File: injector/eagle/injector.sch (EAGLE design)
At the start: 30 parts, among them U1 ATMEGA328, U2 ATA6631, U3 ATA6631, X1 16MHz

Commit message: Renamed proxy to injector.
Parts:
- C1, C3, C4, C6, C7, C8, C9: device proxy:C-USC0805 -> injector:C-USC0805
- C2: device proxy:CPOL-USUD-6,3X5,8 -> injector:CPOL-USUD-6,3X5,8
- C5: device proxy:CPOL-USA/3216-18R -> injector:CPOL-USA/3216-18R
- D2, D3, D6, D9: device proxy:SMF5.0AT1 -> injector:SMF5.0AT1
- F1: device proxy:FUSE -> injector:FUSE
- J3: device proxy:PINHD-1X6 -> injector:PINHD-1X6
- JP1, JP3: device proxy:PINHD-1X3 -> injector:PINHD-1X3
- JP2: device proxy:PINHD-2X3 -> injector:PINHD-2X3
- LED1, LED2: device proxy:LED -> injector:LED
- R1, R2, R3, R4, R5, R9: device proxy:R-US_R0805 -> injector:R-US_R0805
- U1: device proxy:ATMEGA328 -> injector:ATMEGA328
- U2, U3: device proxy:ATA6631 -> injector:ATA6631
- X1: device proxy:RESONATORSMD -> injector:RESONATORSMD

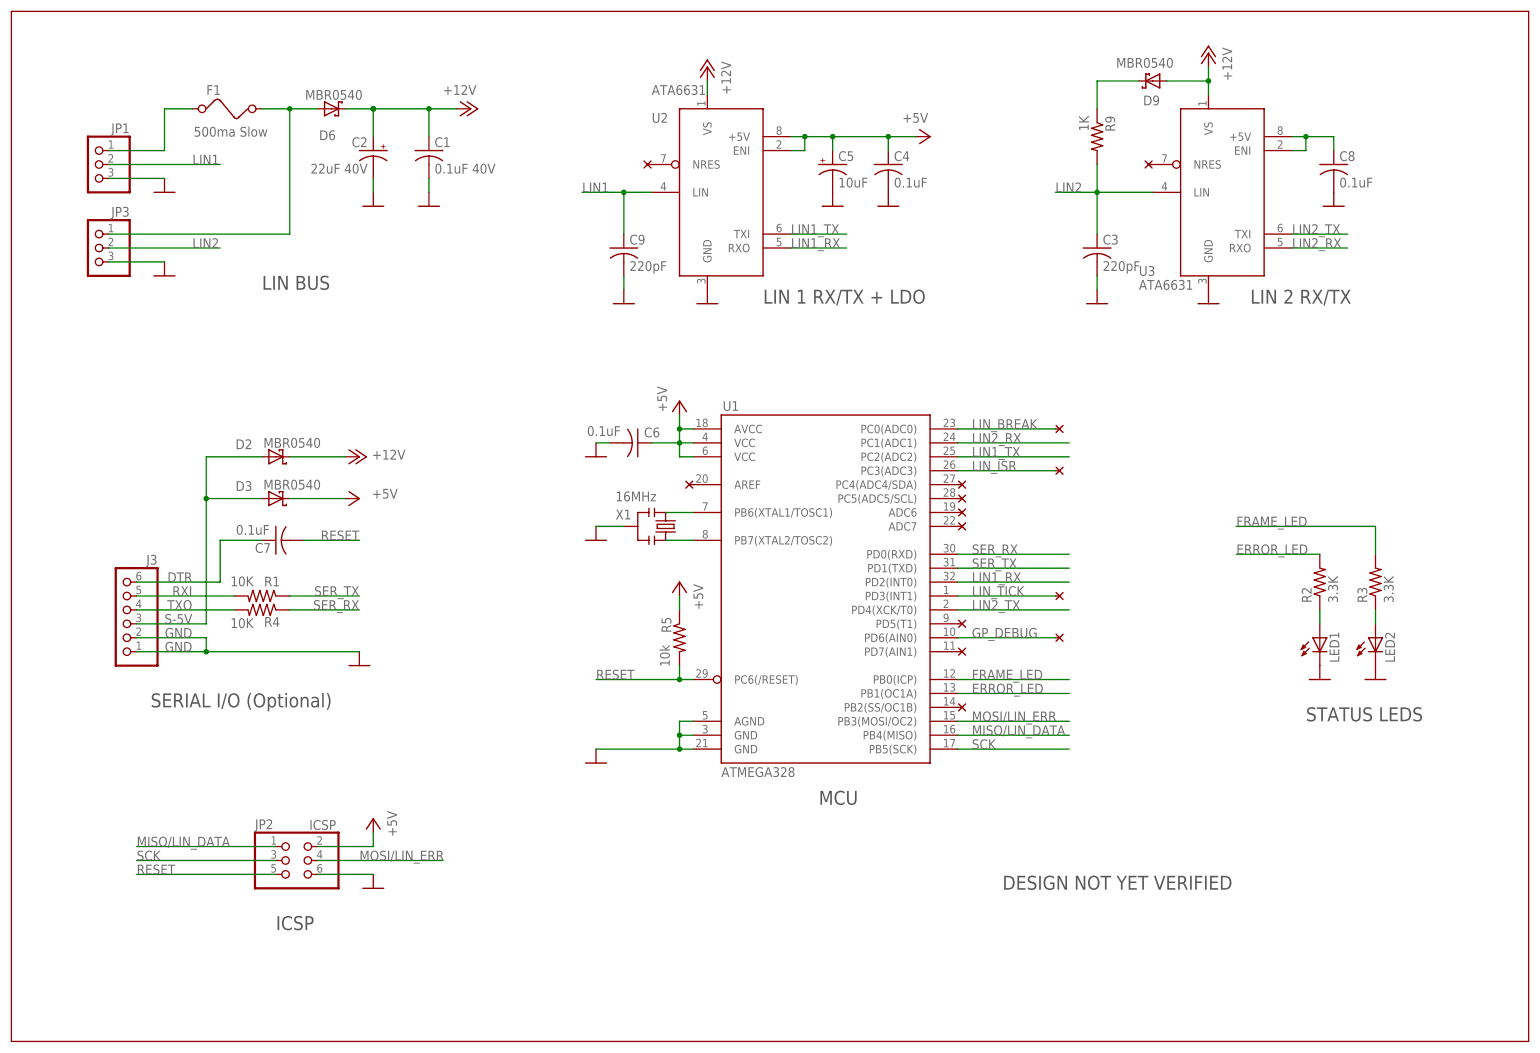
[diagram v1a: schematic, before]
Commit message: Renumber parts.
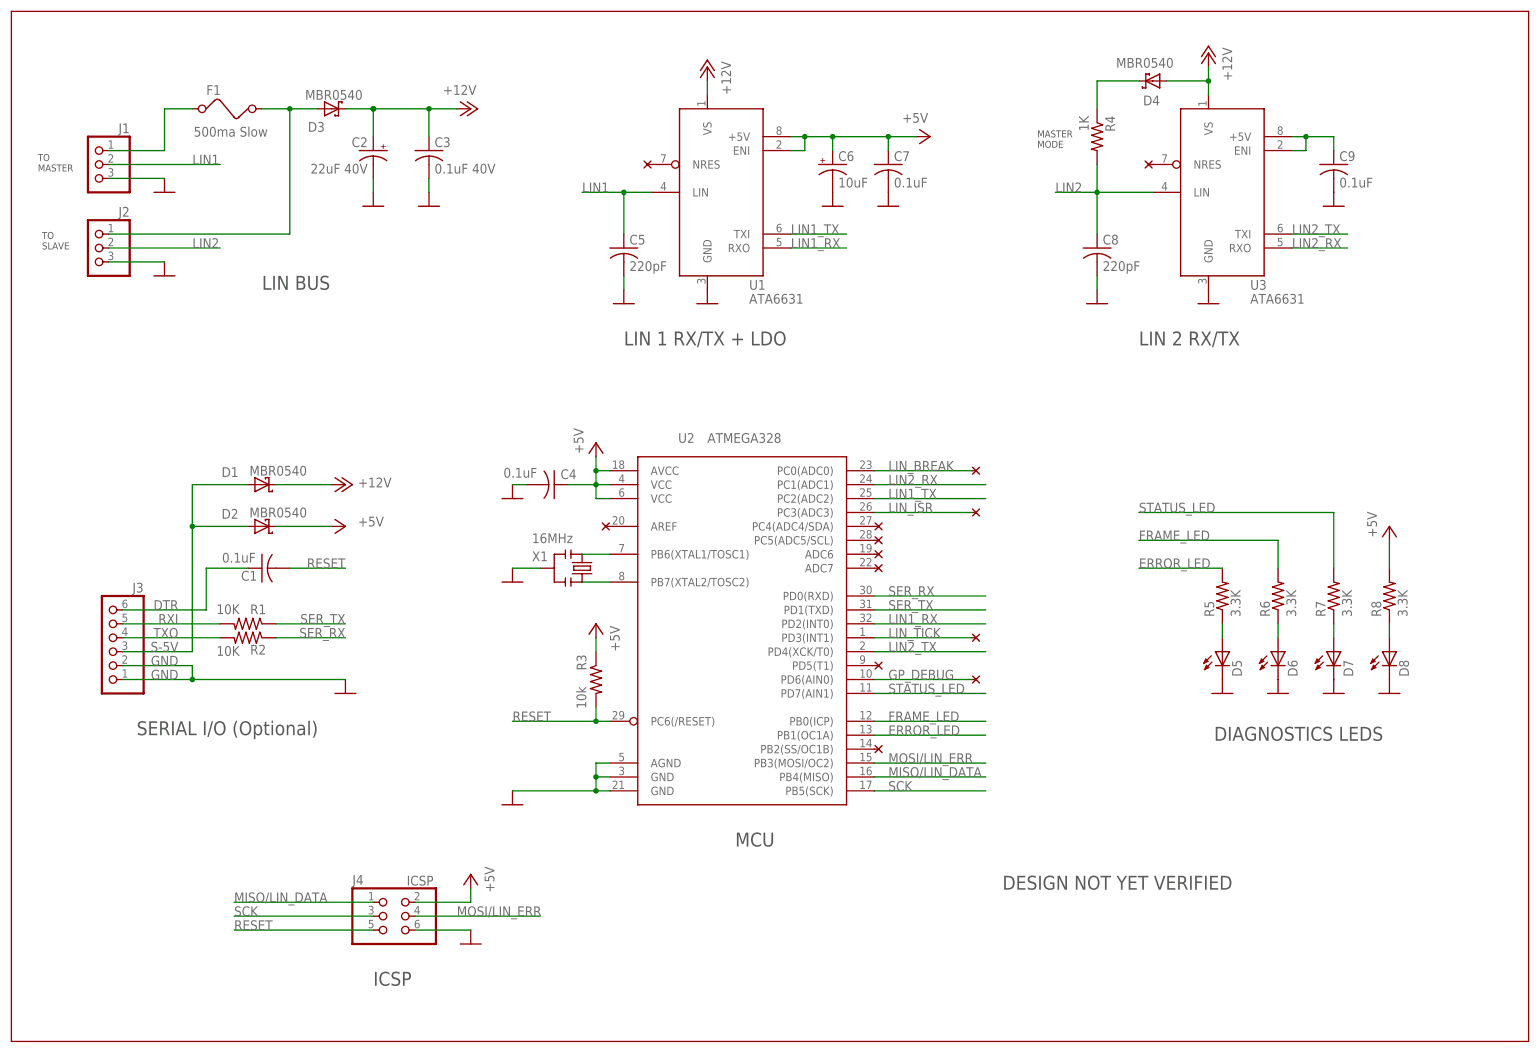
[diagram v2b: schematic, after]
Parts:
- removed JP2: ICSP, injector:PINHD-2X3
- removed LED1, LED2: (no value), injector:LED
- removed R9: 1K, injector:R-US_R0805
- added D1: MBR0540, injector:SMF5.0AT1
- added D5, D7, D8: (no value), injector:LED
- added J4: ICSP, injector:PINHD-2X3
- added R6, R7, R8: 3.3K, injector:R-US_R0805
- C1: value 0.1uF 40V -> 0.1uF
- C3: value 220pF -> 0.1uF 40V
- C5: value 10uF -> 220pF; device injector:CPOL-USA/3216-18R -> injector:C-USC0805
- C6: value 0.1uF -> 10uF; device injector:C-USC0805 -> injector:CPOL-USA/3216-18R
- C8: value 0.1uF -> 220pF
- C9: value 220pF -> 0.1uF
- D6: value MBR0540 -> (none); device injector:SMF5.0AT1 -> injector:LED
- R2: value 3.3K -> 10K
- R3: value 3.3K -> 10k
- R4: value 10K -> 1K
- R5: value 10k -> 3.3K
- U1: value ATMEGA328 -> ATA6631; device injector:ATMEGA328 -> injector:ATA6631
- U2: value ATA6631 -> ATMEGA328; device injector:ATA6631 -> injector:ATMEGA328
- renumbered D9 to D4, JP1 to J1, JP3 to J2
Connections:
- new net N$1: D7.A, R7.1
- new net N$2: D8.A, R8.1
- new net STATUS_LED: R7.2, U2.PD7(AIN1)
- net +12V: now also C3.1, D1.C, D3.C, U1.VS; no longer C1.1, D2.C, D6.C, U2.VS
- net +5V: now also C6.+, C7.1, D2.C, J4.2, R3.1, R8.2, U1.+5V, U1.ENI, U2.AVCC, U2.VCC@1, U2.VCC@2; no longer C5.+, C6.1, D3.C, JP2.2, R5.1, U1.AVCC, U1.VCC@1, U1.VCC@2, U2.+5V, U2.ENI
- net DTR: now also C1.1; no longer C7.1
- net ERROR_LED: now also R5.2, U2.PB1(OC1A); no longer R2.2, U1.PB1(OC1A)
- net FRAME_LED: now also R6.2, U2.PB0(ICP); no longer R3.2, U1.PB0(ICP)
- net GND: now also C5.2, C6.-, C7.2, D5.C, D6.C, D7.C, D8.C, J4.6, U1.GND, U2.AGND, U2.GND@1, U2.GND@2; no longer C1.2, C5.-, C6.2, JP2.6, LED1.C, LED2.C, U1.AGND, U1.GND@1, U1.GND@2, U2.GND
- net GP_DEBUG: now also U2.PD6(AIN0); no longer U1.PD6(AIN0)
- net LIN1: now also C5.1, U1.LIN; no longer C9.1, U2.LIN
- net LIN1_RX: now also U1.RXO, U2.PD2(INT0); no longer U1.PD2(INT0), U2.RXO
- net LIN1_TX: now also U1.TXI, U2.PC2(ADC2); no longer U1.PC2(ADC2), U2.TXI
- net LIN2: now also C8.1, R4.2; no longer C3.1, R9.2
- net LIN2_RX: now also U2.PC1(ADC1); no longer U1.PC1(ADC1)
- net LIN2_TX: now also U2.PD4(XCK/T0); no longer U1.PD4(XCK/T0)
- net LIN_BREAK: now also U2.PC0(ADC0); no longer U1.PC0(ADC0)
- net LIN_ISR: now also U2.PC3(ADC3); no longer U1.PC3(ADC3)
- net LIN_TICK: now also U2.PD3(INT1); no longer U1.PD3(INT1)
- net MISO/LIN_DATA: now also J4.1, U2.PB4(MISO); no longer JP2.1, U1.PB4(MISO)
- net MOSI/LIN_ERR: now also J4.4, U2.PB3(MOSI/OC2); no longer JP2.4, U1.PB3(MOSI/OC2)
- net N$3: now also D6.A, R6.1; no longer LED2.A, R3.1
- net N$4: now also D5.A, R5.1; no longer LED1.A, R2.1
- net N$6: now also D3.A; no longer D6.A
- net N$9: now also R4.1; no longer R9.1
- net RESET: now also C1.2, J4.5, R3.2, U2.PC6(/RESET); no longer C7.2, JP2.5, R5.2, U1.PC6(/RESET)
- net S-5V: now also D1.A; no longer D3.A
- net SCK: now also J4.3, U2.PB5(SCK); no longer JP2.3, U1.PB5(SCK)
- net SECONDARY_5V: now also C9.1; no longer C8.1
- net SER_RX: now also R2.1, U2.PD0(RXD); no longer R4.1, U1.PD0(RXD)
- net SER_TX: now also U2.PD1(TXD); no longer U1.PD1(TXD)
- net TXO: now also R2.2; no longer R4.2
- net XTAL1: now also U2.PB6(XTAL1/TOSC1); no longer U1.PB6(XTAL1/TOSC1)
- net XTAL2: now also U2.PB7(XTAL2/TOSC2); no longer U1.PB7(XTAL2/TOSC2)
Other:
- note added: "DIAGNOSTICS LEDS"
- note added: "MASTER MODE"
- note added: "TO MASTER"
- note added: "TO SLAVE"
- note removed: "STATUS LEDS"
- moved on the sheet: C1, C3, C4, C7, C8, C9, D2, D3, J3, R1, R2, R3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
